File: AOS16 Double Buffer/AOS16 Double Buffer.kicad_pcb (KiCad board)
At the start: 4 copper layers, 50 x 75 mm, 69 parts, among them IC1 SN74AHCT16245DGVR, IC2 SN74AHCT16245DGVR, IC3 SN74AHCT16245DGVR, IC4 SN74AHCT16245DGVR, J1 Conn_01x07_Pin, J2 Conn_02x08_Top_Bottom, J3 Conn_02x08_Top_Bottom, J4 Conn_02x08_Top_Bottom, J5 Conn_02x08_Top_Bottom, U1 74AHCT1G08, U2 74AHCT1G08, U3 74AHCT1G32, U4 74AHCT1G32, U5 74AHCT1G04, U6 74AHCT1G04, U7 74LVC157, U8 71016S12PHG8

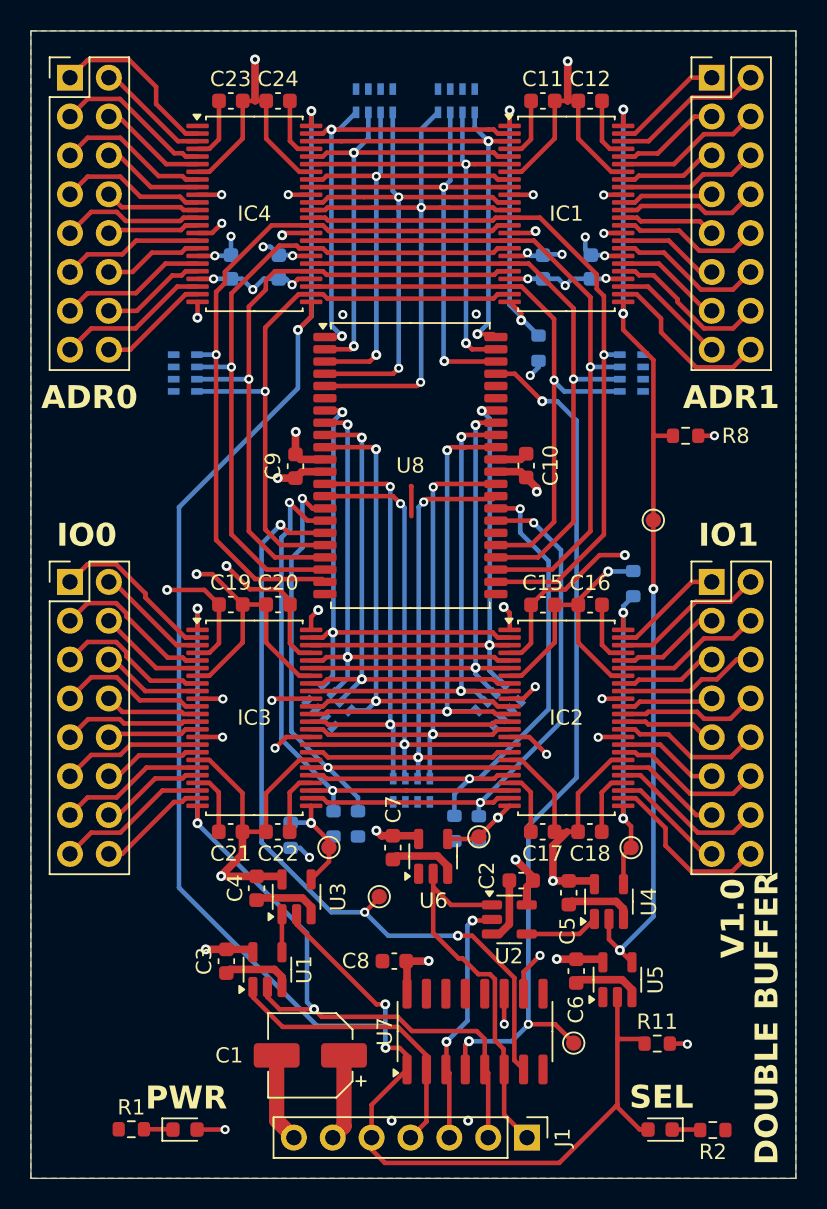
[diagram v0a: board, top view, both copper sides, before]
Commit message: Fixed silkscreen on ALU and Double Buffer
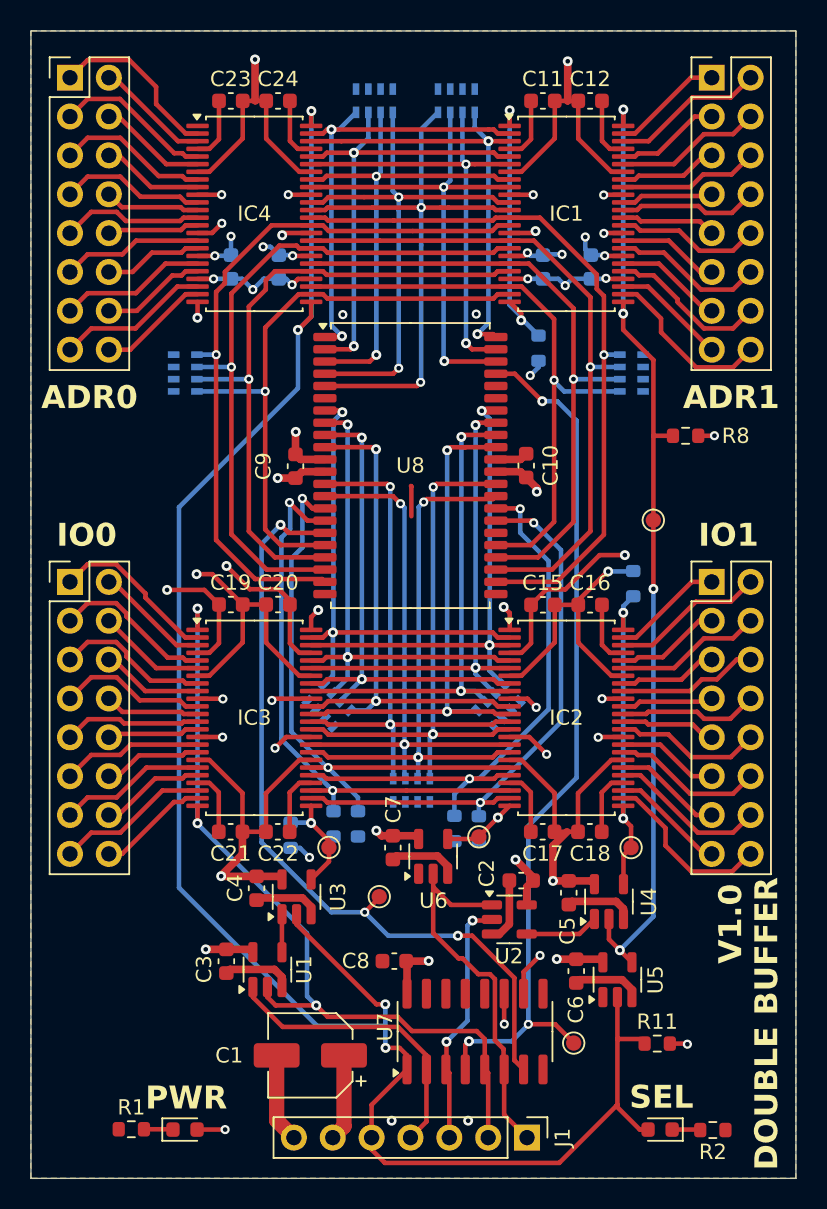
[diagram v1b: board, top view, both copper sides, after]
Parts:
- IC1, IC2, IC3, IC4: value SN74AHCT16245DGVR -> SN74AHCT16245DGGR
